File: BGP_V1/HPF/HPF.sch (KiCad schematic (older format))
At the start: 12 parts, among them P1 CONN_01X05, P2 CONN_01X06, U1 OPA2170

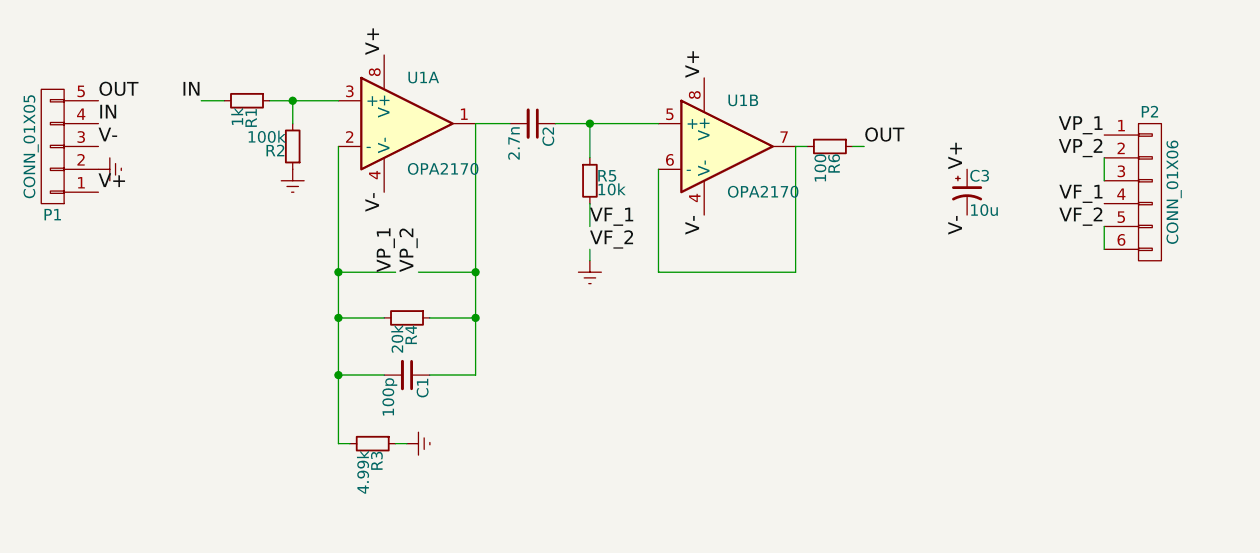
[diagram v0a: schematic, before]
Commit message: Pot fixups for silkscreen overlap
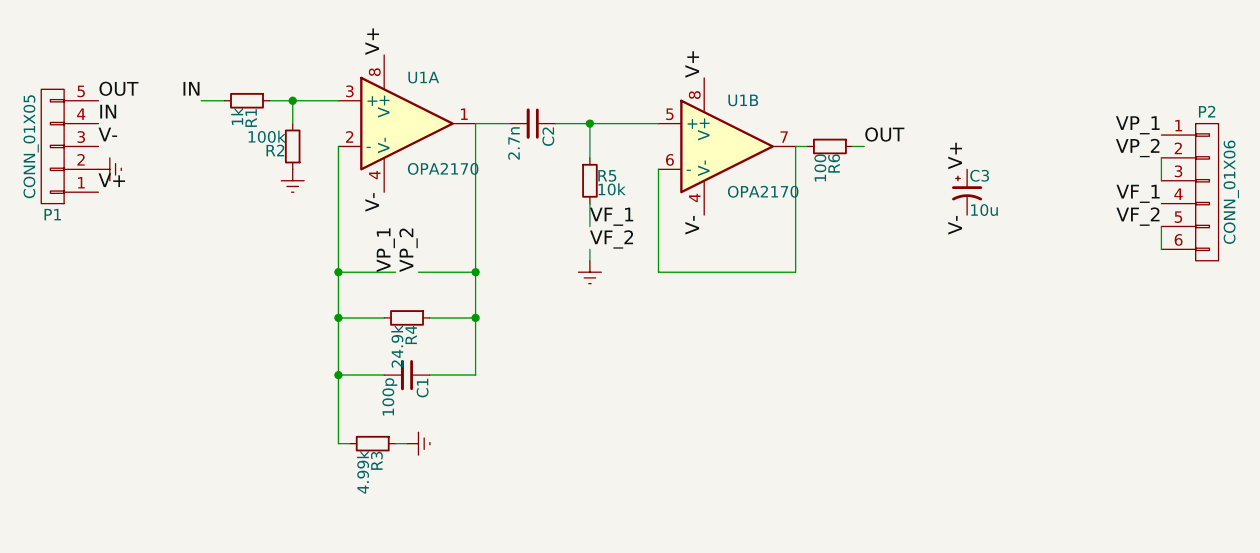
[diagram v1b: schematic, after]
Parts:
- R4: value 20k -> 24.9k
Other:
- moved on the sheet: P2
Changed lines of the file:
@@
 P 5350 4050
 F 0 "R4" H 5380 4070 50  0000 L CNN
-F 1 "20k" H 5380 4010 50  0000 L CNN
+F 1 "24.9k" H 5380 4010 50  0000 L CNN
 F 2 "Resistors_SMD:R_0603_HandSoldering" H 5350 4050 50  0001 C CNN
 F 3 "" H 5350 4050 50  0000 C CNN
@@
 L CONN_01X06 P2
 U 1 1 5A532055
-P 8600 3500
-F 0 "P2" H 8600 3850 50  0000 C CNN
-F 1 "CONN_01X06" V 8700 3500 50  0000 C CNN
-F 2 "LIBS:Potentiometer_Alps_RK097_Double_Vertical_Dual_Shaft" H 8600 3500 50  0001 C CNN
-F 3 "" H 8600 3500 50  0000 C CNN
-	1    8600 3500
+P 8850 3500
+F 0 "P2" H 8850 3850 50  0000 C CNN
+F 1 "CONN_01X06" V 8950 3500 50  0000 C CNN
+F 2 "LIBS:Potentiometer_Alps_RK097_Double_Vertical_Dual_Shaft" H 8850 3500 50  0001 C CNN
+F 3 "" H 8850 3500 50  0000 C CNN
+	1    8850 3500
 	1    0    0    -1
 $EndComp
 Wire Wire Line
-	8400 3350 8400 3450
-Text Label 8400 3250 2    60   ~ 0
+	8650 3350 8650 3450
+Text Label 8650 3250 2    60   ~ 0
 VP_1
-Text Label 8400 3350 2    60   ~ 0
+Text Label 8650 3350 2    60   ~ 0
 VP_2
 Wire Wire Line
-	8400 3750 8400 3650
-Text Label 8400 3550 2    60   ~ 0
+	8650 3750 8650 3650
+Text Label 8650 3550 2    60   ~ 0
 VF_1
-Text Label 8400 3650 2    60   ~ 0
+Text Label 8650 3650 2    60   ~ 0
 VF_2
 $EndSCHEMATC

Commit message: Concentric pot fixups for 0_BT Stack and 1_HPF
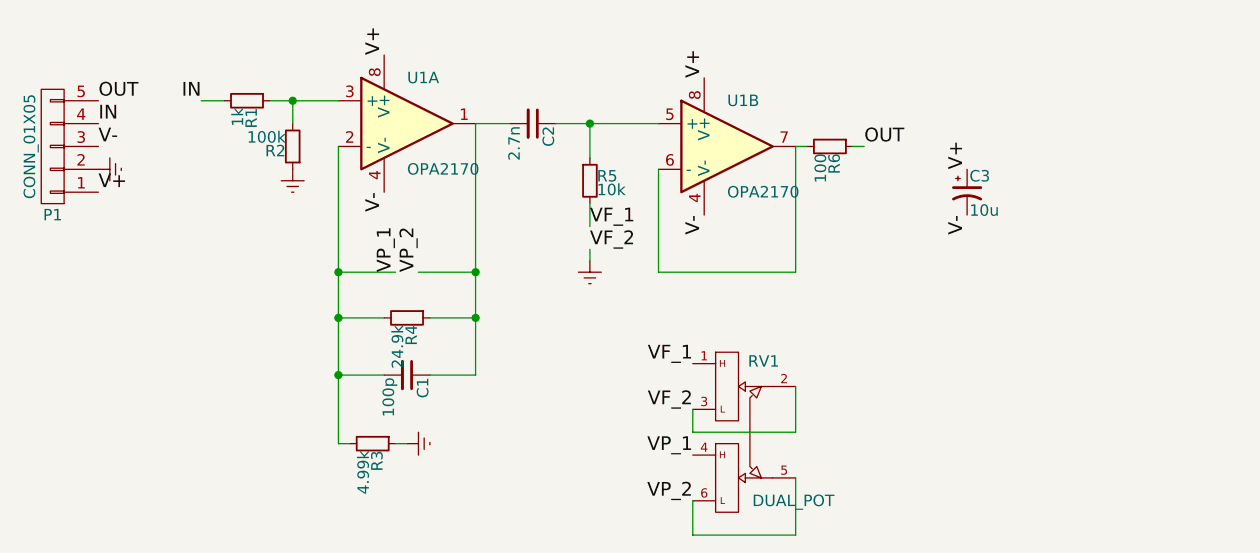
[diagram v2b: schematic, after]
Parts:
- removed P2: CONN_01X06, LIBS:Potentiometer_Alps_RK097_Double_Vertical_Dual_Shaft, symbol CONN_01X06
- added RV1: DUAL_POT, LIBS:Potentiometer_Alps_RK097_Double_Vertical_Dual_Shaft, symbol DUAL_POT
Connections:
- net Earth: now also RV1.2, RV1.3
- net VF_1: now also RV1.1
- net VP_1: now also RV1.4
- net VP_2: now also RV1.5, RV1.6
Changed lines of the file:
@@
 	4850 3200 4850 3100
 Connection ~ 4850 3100
+Text Label 6600 4650 2    60   ~ 0
+VP_1
+Text Label 6600 4850 2    60   ~ 0
+VP_2
+Text Label 6600 4250 2    60   ~ 0
+VF_1
+Text Label 6600 4450 2    60   ~ 0
+VF_2
 $Comp
-L CONN_01X06 P2
-U 1 1 5A532055
-P 8850 3500
-F 0 "P2" H 8850 3850 50  0000 C CNN
-F 1 "CONN_01X06" V 8950 3500 50  0000 C CNN
-F 2 "LIBS:Potentiometer_Alps_RK097_Double_Vertical_Dual_Shaft" H 8850 3500 50  0001 C CNN
-F 3 "" H 8850 3500 50  0000 C CNN
-	1    8850 3500
+L DUAL_POT RV1
+U 1 1 5A5819B7
+P 6750 4550
+F 0 "RV1" H 6910 4860 50  0000 C CNN
+F 1 "DUAL_POT" H 7040 4250 50  0000 C CNN
+F 2 "LIBS:Potentiometer_Alps_RK097_Double_Vertical_Dual_Shaft" H 6750 4550 50  0001 C CNN
+F 3 "" H 6750 4550 50  0000 C CNN
+	1    6750 4550
 	1    0    0    -1
 $EndComp
 Wire Wire Line
-	8650 3350 8650 3450
-Text Label 8650 3250 2    60   ~ 0
-VP_1
-Text Label 8650 3350 2    60   ~ 0
-VP_2
+	7050 4750 7050 5000
 Wire Wire Line
-	8650 3750 8650 3650
-Text Label 8650 3550 2    60   ~ 0
-VF_1
-Text Label 8650 3650 2    60   ~ 0
-VF_2
+	7050 5000 6600 5000
+Wire Wire Line
+	6600 5000 6600 4850
+Wire Wire Line
+	7050 4350 7050 4550
+Wire Wire Line
+	7050 4550 6600 4550
+Wire Wire Line
+	6600 4550 6600 4450
 $EndSCHEMATC

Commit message: Some cleanup and gerbers updated to reflect this
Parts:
- C3: footprint Capacitors_SMD:C_1206_HandSoldering -> Capacitors_SMD:C_0805_HandSoldering
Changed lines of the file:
@@
 F 0 "C3" H 7810 3570 50  0000 L CNN
 F 1 "10u" H 7810 3420 50  0000 L CNN
-F 2 "Capacitors_SMD:C_1206_HandSoldering" H 7800 3500 50  0001 C CNN
+F 2 "Capacitors_SMD:C_0805_HandSoldering" H 7800 3500 50  0001 C CNN
 F 3 "" H 7800 3500 50  0000 C CNN
 	1    7800 3500

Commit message: Changed 1_HPF to use ALPHA 12mm pot.
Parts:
- RV1: footprint LIBS:Potentiometer_Alps_RK097_Double_Vertical_Dual_Shaft -> LIBS:Potentiometer_Alpha_Double_Vertical_Dual_Shaft
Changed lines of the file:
@@
 F 0 "RV1" H 6910 4860 50  0000 C CNN
 F 1 "DUAL_POT" H 7040 4250 50  0000 C CNN
-F 2 "LIBS:Potentiometer_Alps_RK097_Double_Vertical_Dual_Shaft" H 6750 4550 50  0001 C CNN
+F 2 "LIBS:Potentiometer_Alpha_Double_Vertical_Dual_Shaft" H 6750 4550 50  0001 C CNN
 F 3 "" H 6750 4550 50  0000 C CNN
 	1    6750 4550
